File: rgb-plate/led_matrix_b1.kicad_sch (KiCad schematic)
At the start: 64 parts

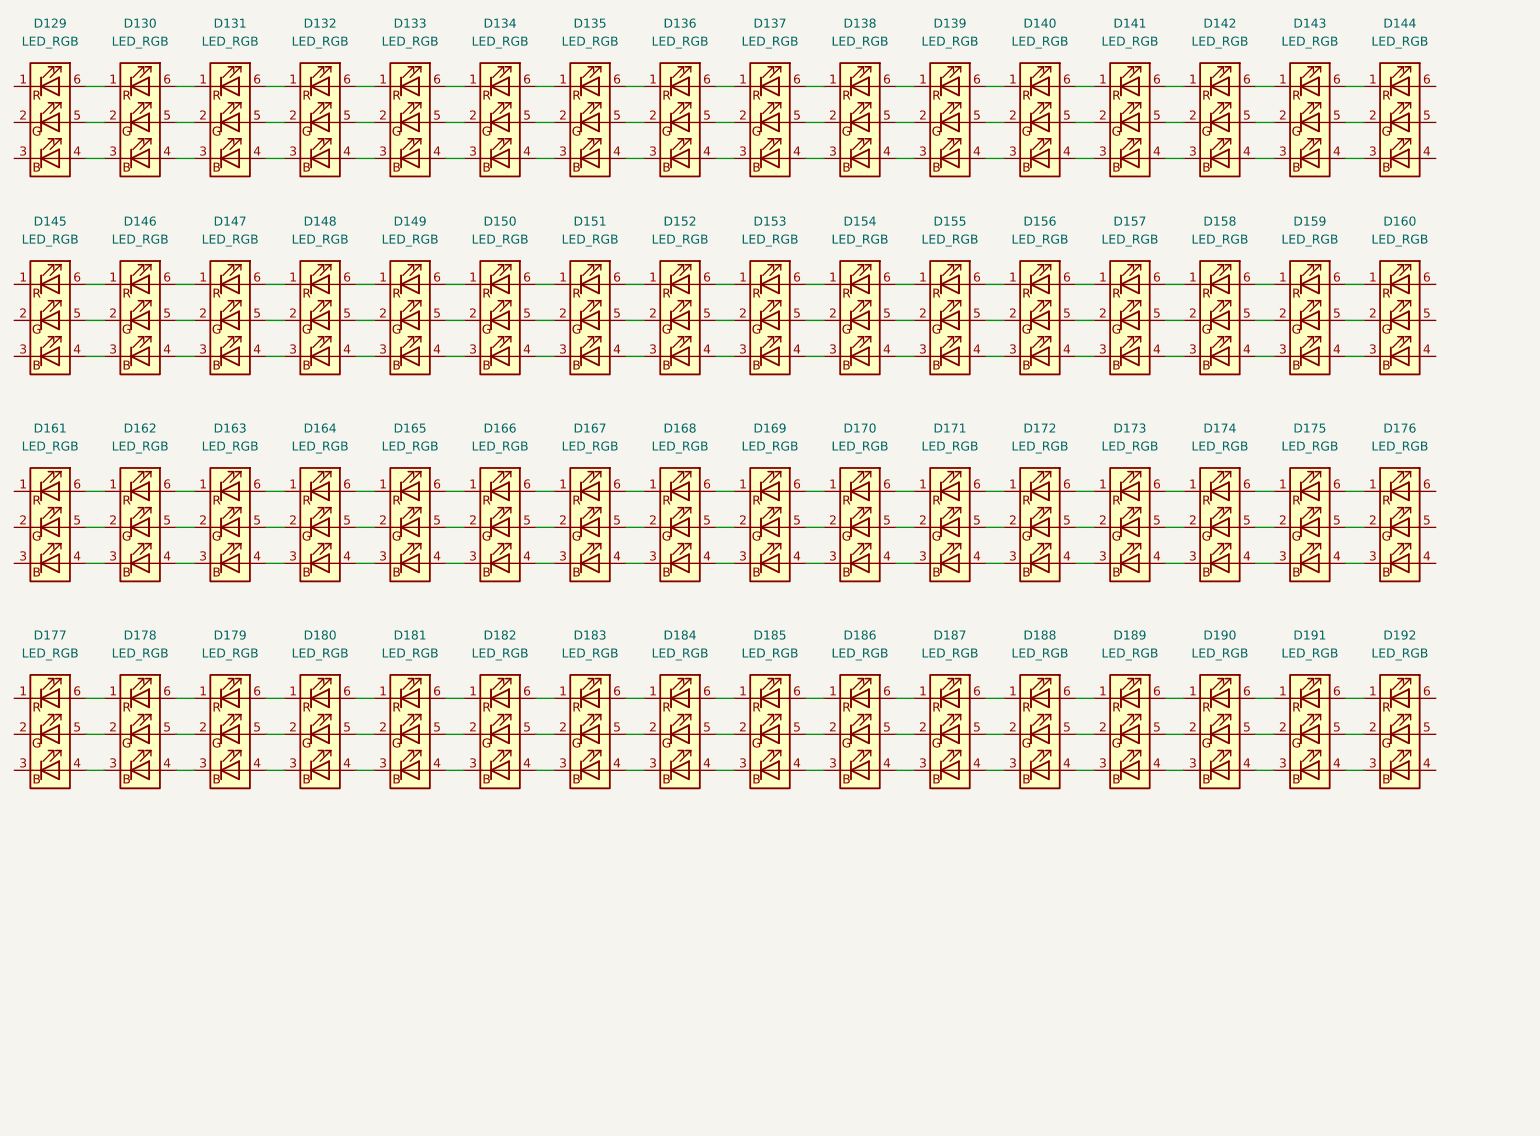
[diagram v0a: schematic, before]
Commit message: initial layout on single board, may need to split up
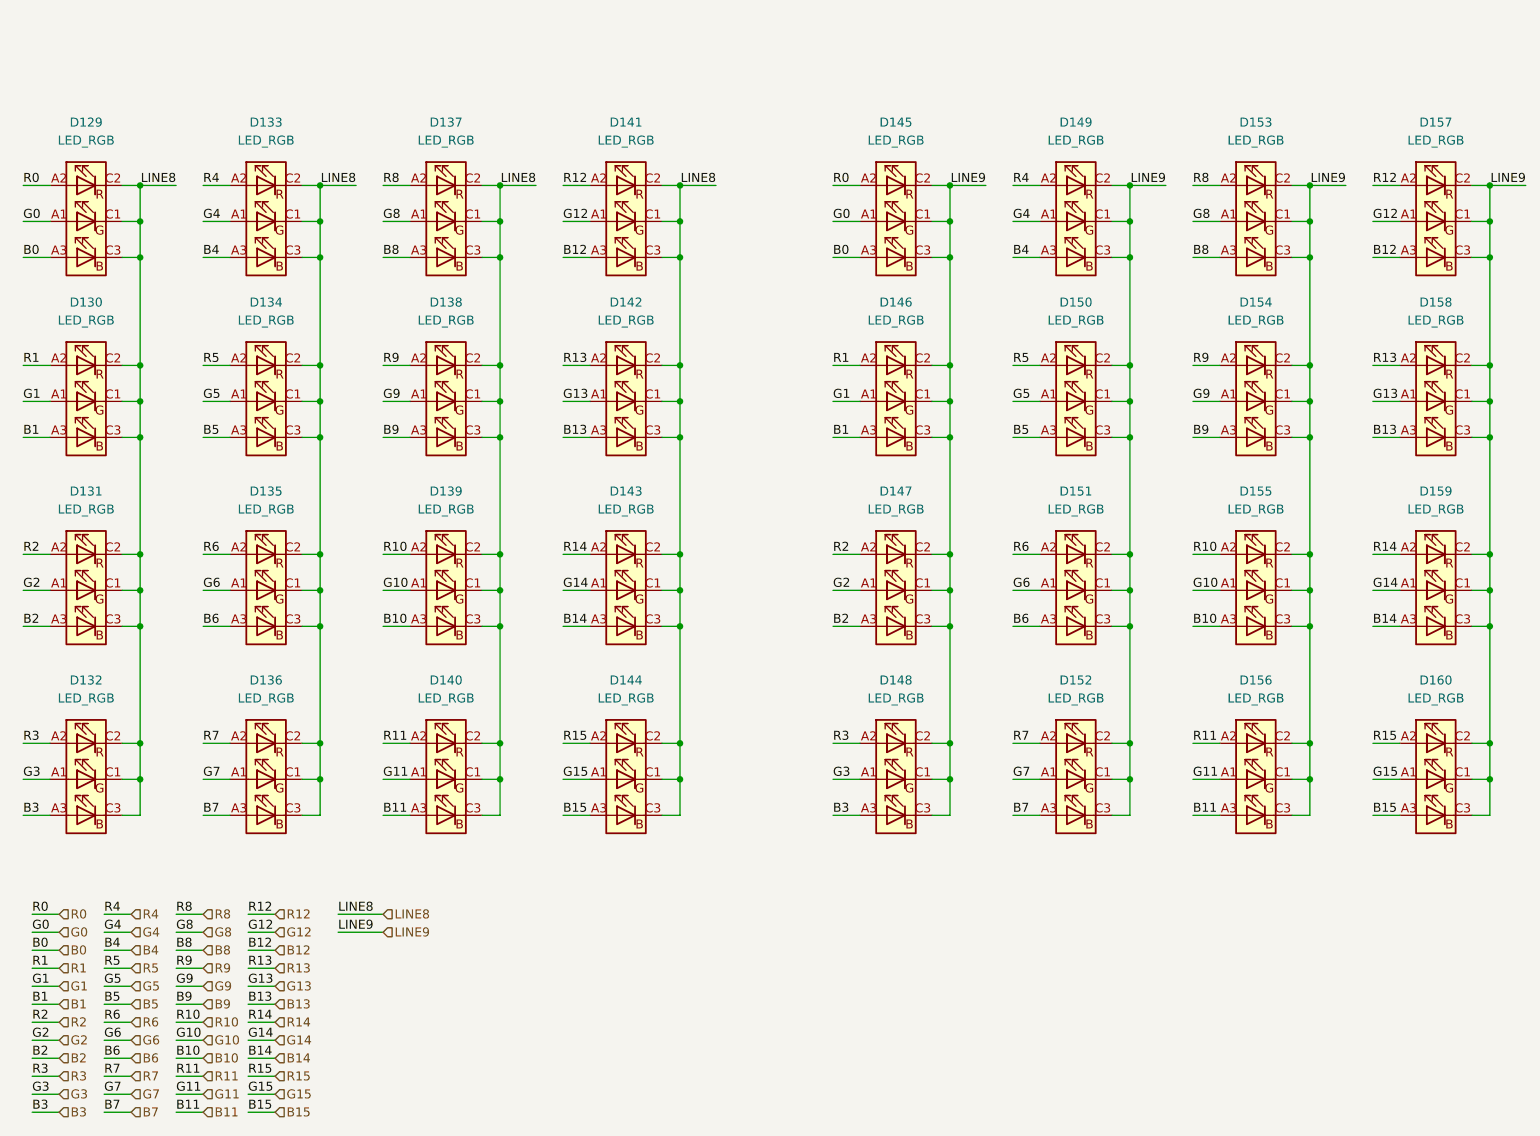
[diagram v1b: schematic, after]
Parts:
- removed D129, D130, D131, D132, D133, D134, D135, D136, D137, D138, D139, D140, D141, D142, D143, D144, D145, D146, D147, D148, D149, D150, D151, D152, D153, D154, D155, D156, D157, D158, D159, D160, D161, D162, D163, D164, D165, D166, D167, D168, D169, D170, D171, D172, D173, D174, D175, D176, D177, D178, D179, D180, D181, D182, D183, D184, D185, D186, D187, D188, D189, D190, D191, D192: LED_RGB, symbol Device:LED_RGB
- added D129, D130, D131, D132, D133, D134, D135, D136, D137, D138, D139, D140, D141, D142, D143, D144, D145, D146, D147, D148, D149, D150, D151, D152, D153, D154, D155, D156, D157, D158, D159, D160: LED_RGB, LRTBGVSR-4U4V-JW+8A8B-D8-3S4U-7Z:LRTBGVSR4U4VJW8A8BD83S4U7Z, symbol LRTBGVSR-4U4V-JW+8A8B-D8-3S4U-:LED_RGB
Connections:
- new net B0: D129.A3 (BA), D145.A3 (BA)
- new net B1: D130.A3 (BA), D146.A3 (BA)
- new net B10: D139.A3 (BA), D155.A3 (BA)
- new net B11: D140.A3 (BA), D156.A3 (BA)
- new net B12: D141.A3 (BA), D157.A3 (BA)
- new net B13: D142.A3 (BA), D158.A3 (BA)
- new net B14: D143.A3 (BA), D159.A3 (BA)
- new net B15: D144.A3 (BA), D160.A3 (BA)
- new net B2: D131.A3 (BA), D147.A3 (BA)
- new net B3: D132.A3 (BA), D148.A3 (BA)
- new net B4: D133.A3 (BA), D149.A3 (BA)
- new net B5: D134.A3 (BA), D150.A3 (BA)
- new net B6: D135.A3 (BA), D151.A3 (BA)
- new net B7: D136.A3 (BA), D152.A3 (BA)
- new net B8: D137.A3 (BA), D153.A3 (BA)
- new net B9: D138.A3 (BA), D154.A3 (BA)
- new net G0: D129.A1 (GA), D145.A1 (GA)
- new net G1: D130.A1 (GA), D146.A1 (GA)
- new net G10: D139.A1 (GA), D155.A1 (GA)
- new net G11: D140.A1 (GA), D156.A1 (GA)
- new net G12: D141.A1 (GA), D157.A1 (GA)
- new net G13: D142.A1 (GA), D158.A1 (GA)
- new net G14: D143.A1 (GA), D159.A1 (GA)
- new net G15: D144.A1 (GA), D160.A1 (GA)
- new net G2: D131.A1 (GA), D147.A1 (GA)
- new net G3: D132.A1 (GA), D148.A1 (GA)
- new net G4: D133.A1 (GA), D149.A1 (GA)
- new net G5: D134.A1 (GA), D150.A1 (GA)
- new net G6: D135.A1 (GA), D151.A1 (GA)
- new net G7: D136.A1 (GA), D152.A1 (GA)
- new net G8: D137.A1 (GA), D153.A1 (GA)
- new net G9: D138.A1 (GA), D154.A1 (GA)
- new net LINE8: D129.C1 (GK), D129.C2 (RK), D129.C3 (BK), D130.C1 (GK), D130.C2 (RK), D130.C3 (BK), D131.C1 (GK), D131.C2 (RK), D131.C3 (BK), D132.C1 (GK), D132.C2 (RK), D132.C3 (BK), D133.C1 (GK), D133.C2 (RK), D133.C3 (BK), D134.C1 (GK), D134.C2 (RK), D134.C3 (BK), D135.C1 (GK), D135.C2 (RK), D135.C3 (BK), D136.C1 (GK), D136.C2 (RK), D136.C3 (BK), D137.C1 (GK), D137.C2 (RK), D137.C3 (BK), D138.C1 (GK), D138.C2 (RK), D138.C3 (BK), D139.C1 (GK), D139.C2 (RK), D139.C3 (BK), D140.C1 (GK), D140.C2 (RK), D140.C3 (BK), D141.C1 (GK), D141.C2 (RK), D141.C3 (BK), D142.C1 (GK), D142.C2 (RK), D142.C3 (BK), D143.C1 (GK), D143.C2 (RK), D143.C3 (BK), D144.C1 (GK), D144.C2 (RK), D144.C3 (BK)
- new net LINE9: D145.C1 (GK), D145.C2 (RK), D145.C3 (BK), D146.C1 (GK), D146.C2 (RK), D146.C3 (BK), D147.C1 (GK), D147.C2 (RK), D147.C3 (BK), D148.C1 (GK), D148.C2 (RK), D148.C3 (BK), D149.C1 (GK), D149.C2 (RK), D149.C3 (BK), D150.C1 (GK), D150.C2 (RK), D150.C3 (BK), D151.C1 (GK), D151.C2 (RK), D151.C3 (BK), D152.C1 (GK), D152.C2 (RK), D152.C3 (BK), D153.C1 (GK), D153.C2 (RK), D153.C3 (BK), D154.C1 (GK), D154.C2 (RK), D154.C3 (BK), D155.C1 (GK), D155.C2 (RK), D155.C3 (BK), D156.C1 (GK), D156.C2 (RK), D156.C3 (BK), D157.C1 (GK), D157.C2 (RK), D157.C3 (BK), D158.C1 (GK), D158.C2 (RK), D158.C3 (BK), D159.C1 (GK), D159.C2 (RK), D159.C3 (BK), D160.C1 (GK), D160.C2 (RK), D160.C3 (BK)
- new net R0: D129.A2 (RA), D145.A2 (RA)
- new net R1: D130.A2 (RA), D146.A2 (RA)
- new net R10: D139.A2 (RA), D155.A2 (RA)
- new net R11: D140.A2 (RA), D156.A2 (RA)
- new net R12: D141.A2 (RA), D157.A2 (RA)
- new net R13: D142.A2 (RA), D158.A2 (RA)
- new net R14: D143.A2 (RA), D159.A2 (RA)
- new net R15: D144.A2 (RA), D160.A2 (RA)
- new net R2: D131.A2 (RA), D147.A2 (RA)
- new net R3: D132.A2 (RA), D148.A2 (RA)
- new net R4: D133.A2 (RA), D149.A2 (RA)
- new net R5: D134.A2 (RA), D150.A2 (RA)
- new net R6: D135.A2 (RA), D151.A2 (RA)
- new net R7: D136.A2 (RA), D152.A2 (RA)
- new net R8: D137.A2 (RA), D153.A2 (RA)
- new net R9: D138.A2 (RA), D154.A2 (RA)
